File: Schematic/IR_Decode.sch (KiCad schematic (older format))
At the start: 5 parts, among them IC12 74LS574, IC13 74LS161-wkt, IC14 AT27C1024-70PU, IC15 74LS139, IC16 74LS138

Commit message: Fixed up some schematic DCN mistakes and also a few minor typos and diagram issues.
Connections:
- net GND: now also IC12.1 (OE), IC12.10 (Gnd), IC13.8 (Gnd), IC14.11 (GND), IC14.2 (~CE), IC14.20 (~OE), IC14.30 (GND_1), IC14.34 (A12), IC14.35 (A13), IC14.36 (A14), IC14.37 (A15), IC16.4 (E1), IC16.5 (E2)
- removed net GNDREF: IC12.1 (OE), IC12.10 (Gnd), IC13.8 (Gnd), IC14.11 (GND), IC14.2 (~CE), IC14.20 (~OE), IC14.30 (GND_1), IC14.34 (A12), IC14.35 (A13), IC14.36 (A14), IC14.37 (A15), IC15.1 (E), IC16.4 (E1), IC16.5 (E2)
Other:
- note added: "ALUop"
- note added: "DataBus"
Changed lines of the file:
@@
 Entry Wire Line
 	6400 3600 6500 3700
-Text GLabel 6700 4300 2    60   Input ~ 0
-ALUop
+Text GLabel 6600 4300 2    60   Input ~ 0
+Op[0..4]
 Text Label 6000 4000 0    60   ~ 0
 Op0
@@
 	6500 3700 6500 4300
 Wire Bus Line
-	6500 4300 6700 4300
+	6500 4300 6600 4300
 Wire Wire Line
 	5900 3600 6400 3600
@@
 Wire Bus Line
 	1700 2500 1200 2500
-Text GLabel 1200 2500 0    60   Input ~ 0
-DataBus
 Text Label 1850 3600 0    60   ~ 0
 d0
@@
 uSequence\n  Counter
 $Comp
-L GNDREF #PWR043
+L GNDREF #PWR033
 U 1 1 5C99C89C
 P 7250 2250
-F 0 "#PWR043" H 7250 2000 50  0001 C CNN
+F 0 "#PWR033" H 7250 2000 50  0001 C CNN
 F 1 "GNDREF" H 7250 2100 50  0000 C CNN
 F 2 "" H 7250 2250 50  0001 C CNN
@@
 $EndComp
 $Comp
-L GNDREF #PWR044
+L GNDREF #PWR034
 U 1 1 5C99C8B7
 P 3750 3900
-F 0 "#PWR044" H 3750 3650 50  0001 C CNN
+F 0 "#PWR034" H 3750 3650 50  0001 C CNN
 F 1 "GNDREF" H 3750 3750 50  0000 C CNN
 F 2 "" H 3750 3900 50  0001 C CNN
@@
 $EndComp
 $Comp
-L GNDREF #PWR045
+L GNDREF #PWR035
 U 1 1 5C99C8CB
 P 3750 5700
-F 0 "#PWR045" H 3750 5450 50  0001 C CNN
+F 0 "#PWR035" H 3750 5450 50  0001 C CNN
 F 1 "GNDREF" H 3750 5550 50  0000 C CNN
 F 2 "" H 3750 5700 50  0001 C CNN
@@
 $EndComp
 $Comp
-L VCC #PWR046
+L VCC #PWR036
 U 1 1 5C99C8DE
 P 3750 3800
-F 0 "#PWR046" H 3750 3650 50  0001 C CNN
+F 0 "#PWR036" H 3750 3650 50  0001 C CNN
 F 1 "VCC" H 3750 3950 50  0000 C CNN
 F 2 "" H 3750 3800 50  0001 C CNN
@@
 $EndComp
 $Comp
-L VCC #PWR047
+L VCC #PWR037
 U 1 1 5C99C8F9
 P 3750 5600
-F 0 "#PWR047" H 3750 5450 50  0001 C CNN
+F 0 "#PWR037" H 3750 5450 50  0001 C CNN
 F 1 "VCC" H 3750 5750 50  0000 C CNN
 F 2 "" H 3750 5600 50  0001 C CNN
@@
 $EndComp
 $Comp
-L VCC #PWR048
+L VCC #PWR038
 U 1 1 5C99C910
 P 6150 1950
-F 0 "#PWR048" H 6150 1800 50  0001 C CNN
+F 0 "#PWR038" H 6150 1800 50  0001 C CNN
 F 1 "VCC" H 6150 2100 50  0000 C CNN
 F 2 "" H 6150 1950 50  0001 C CNN
@@
 NoConn ~ 2200 5150
 $Comp
-L VCC #PWR049
+L VCC #PWR039
 U 1 1 5C99CB09
 P 1850 5150
-F 0 "#PWR049" H 1850 5000 50  0001 C CNN
+F 0 "#PWR039" H 1850 5000 50  0001 C CNN
 F 1 "VCC" H 1850 5300 50  0000 C CNN
 F 2 "" H 1850 5150 50  0001 C CNN
@@
 JumpZ
 $Comp
-L GNDREF #PWR050
+L GNDREF #PWR040
 U 1 1 5C99F486
 P 4150 2700
-F 0 "#PWR050" H 4150 2450 50  0001 C CNN
+F 0 "#PWR040" H 4150 2450 50  0001 C CNN
 F 1 "GNDREF" H 4150 2550 50  0000 C CNN
 F 2 "" H 4150 2700 50  0001 C CNN
@@
 NoConn ~ 4800 2250
 $Comp
-L VCC #PWR051
+L VCC #PWR041
 U 1 1 5C99F6F5
 P 4400 1900
-F 0 "#PWR051" H 4400 1750 50  0001 C CNN
+F 0 "#PWR041" H 4400 1750 50  0001 C CNN
 F 1 "VCC" H 4400 2050 50  0000 C CNN
 F 2 "" H 4400 1900 50  0001 C CNN
@@
 $EndComp
 Wire Wire Line
-	4800 2150 4400 2150
-Wire Wire Line
-	4400 2150 4400 1900
+	4400 2150 4800 2150
+Wire Wire Line
+	4400 1900 4400 2150
 $Comp
 L 74LS139 IC15
@@
 Text Notes 8750 3400 0    60   ~ 0
 Databus\nWriter\ndemux
-Text Notes 8550 5650 0    60   ~ 0
+Text Notes 8600 5750 0    60   ~ 0
 Databus\nReader\ndemux
 $Comp
-L GNDREF #PWR052
+L GNDREF #PWR042
 U 1 1 5C99920E
-P 7850 3550
-F 0 "#PWR052" H 7850 3300 50  0001 C CNN
-F 1 "GNDREF" H 7850 3400 50  0000 C CNN
-F 2 "" H 7850 3550 50  0001 C CNN
-F 3 "" H 7850 3550 50  0001 C CNN
-	1    7850 3550
-	1    0    0    -1
-$EndComp
-Wire Wire Line
-	8050 3550 7850 3550
+P 8000 3900
+F 0 "#PWR042" H 8000 3650 50  0001 C CNN
+F 1 "GNDREF" H 8000 3750 50  0000 C CNN
+F 2 "" H 8000 3900 50  0001 C CNN
+F 3 "" H 8000 3900 50  0001 C CNN
+	1    8000 3900
+	1    0    0    -1
+$EndComp
 $Comp
 L 74LS138 IC16
 U 1 1 5C9992C4
 P 8700 4900
-F 0 "IC16" H 8700 5500 50  0000 C CNN
-F 1 "74LS138" H 8700 5400 50  0000 C CNN
+F 0 "IC16" H 8700 5700 50  0000 C CNN
+F 1 "74LS138" H 8700 5600 50  0000 C CNN
 F 2 "" H 8700 4900 50  0001 C CNN
 F 3 "" H 8700 4900 50  0001 C CNN
@@
 	7150 4550 8100 4550
 $Comp
-L GNDREF #PWR053
+L GNDREF #PWR043
 U 1 1 5C99955D
-P 7850 5250
-F 0 "#PWR053" H 7850 5000 50  0001 C CNN
-F 1 "GNDREF" H 7850 5100 50  0000 C CNN
-F 2 "" H 7850 5250 50  0001 C CNN
-F 3 "" H 7850 5250 50  0001 C CNN
-	1    7850 5250
+P 7850 5550
+F 0 "#PWR043" H 7850 5300 50  0001 C CNN
+F 1 "GNDREF" H 7850 5400 50  0000 C CNN
+F 2 "" H 7850 5550 50  0001 C CNN
+F 3 "" H 7850 5550 50  0001 C CNN
+	1    7850 5550
 	1    0    0    -1
 $EndComp
@@
 Connection ~ 8000 5250
 $Comp
-L VCC #PWR054
+L VCC #PWR044
 U 1 1 5C999650
 P 7850 5050
-F 0 "#PWR054" H 7850 4900 50  0001 C CNN
+F 0 "#PWR044" H 7850 4900 50  0001 C CNN
 F 1 "VCC" H 7850 5200 50  0000 C CNN
 F 2 "" H 7850 5050 50  0001 C CNN
@@
 	8100 5050 7850 5050
 $Comp
-L GNDREF #PWR055
+L GNDREF #PWR045
 U 1 1 5C9996EE
 P 2000 3900
-F 0 "#PWR055" H 2000 3650 50  0001 C CNN
+F 0 "#PWR045" H 2000 3650 50  0001 C CNN
 F 1 "GNDREF" H 2000 3750 50  0000 C CNN
 F 2 "" H 2000 3900 50  0001 C CNN
@@
 Wire Wire Line
 	4800 2700 4650 2700
+Text GLabel 1200 2500 0    60   Input ~ 0
+d[0..7]
+Text Notes 1300 2450 0    60   ~ 0
+DataBus
+Text Notes 6200 4200 0    60   ~ 0
+ALUop
+$Comp
+L VCC #PWR046
+U 1 1 5C9AFDC5
+P 9100 4300
+F 0 "#PWR046" H 9100 4150 50  0001 C CNN
+F 1 "VCC" H 9100 4450 50  0000 C CNN
+F 2 "" H 9100 4300 50  0001 C CNN
+F 3 "" H 9100 4300 50  0001 C CNN
+	1    9100 4300
+	1    0    0    -1
+$EndComp
+Wire Wire Line
+	8700 4450 8700 4300
+Wire Wire Line
+	8700 4300 9100 4300
+Wire Wire Line
+	7850 5550 7850 5250
+Wire Wire Line
+	8700 5350 8700 5450
+Wire Wire Line
+	8700 5450 7850 5450
+Connection ~ 7850 5450
+$Comp
+L VCC #PWR047
+U 1 1 5C9B044B
+P 7700 3500
+F 0 "#PWR047" H 7700 3350 50  0001 C CNN
+F 1 "VCC" H 7700 3650 50  0000 C CNN
+F 2 "" H 7700 3500 50  0001 C CNN
+F 3 "" H 7700 3500 50  0001 C CNN
+	1    7700 3500
+	1    0    0    -1
+$EndComp
+Wire Wire Line
+	8000 3900 8000 3350
+Wire Wire Line
+	8000 3350 8050 3350
+Wire Wire Line
+	8150 3650 8000 3650
+Connection ~ 8000 3650
+Wire Wire Line
+	8150 3550 7700 3550
+Wire Wire Line
+	7700 3550 7700 3500
 $EndSCHEMATC

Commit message: Generated a new schematic of the circuit
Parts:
- IC15: symbol 74LS139 -> 74LS139-RESCUE-Schematic
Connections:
- net GND: now also IC15.1 (E)
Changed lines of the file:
@@
 EESchema Schematic File Version 2
+LIBS:Schematic-rescue
 LIBS:power
 LIBS:device
@@
 LIBS:7400-ic
 LIBS:74LS593
+LIBS:74LS139
 LIBS:Schematic-cache
 EELAYER 25 0
@@
 	4400 1900 4400 2150
 $Comp
-L 74LS139 IC15
+L 74LS139-RESCUE-Schematic IC15
 U 1 1 5C990E8F
 P 8900 3300
+AR Path="/5C990E8F" Ref="IC15"  Part="1"
+AR Path="/5C9850E7/5C990E8F" Ref="IC15"  Part="1"
 F 0 "IC15" H 8900 3850 50  0000 C CNN
 F 1 "74LS139" H 8900 3750 50  0000 C CNN

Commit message: Working on the PCB
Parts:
- IC12: footprint (none) -> Housings_DIP:DIP-20_W7.62mm_Socket
- IC13, IC15, IC16: footprint (none) -> Housings_DIP:DIP-16_W7.62mm_Socket
- IC14: footprint DIP1556W56P254L5232H483Q40N -> Housings_DIP:DIP-40_W25.4mm_Socket
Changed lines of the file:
@@
 F 0 "IC12" H 2900 4100 50  0000 C CNN
 F 1 "74LS574" H 2900 4000 50  0000 C CNN
-F 2 "" H 2900 3400 50  0001 C CNN
+F 2 "Housings_DIP:DIP-20_W7.62mm_Socket" H 2900 3400 50  0001 C CNN
 F 3 "" H 2900 3400 50  0001 C CNN
 	1    2900 3400
@@
 F 0 "IC15" H 8900 3850 50  0000 C CNN
 F 1 "74LS139" H 8900 3750 50  0000 C CNN
-F 2 "" H 8900 3300 50  0001 C CNN
+F 2 "Housings_DIP:DIP-16_W7.62mm_Socket" H 8900 3300 50  0001 C CNN
 F 3 "" H 8900 3300 50  0001 C CNN
 	1    8900 3300
@@
 F 0 "IC13" H 2900 5900 50  0000 C CNN
 F 1 "74LS161-wkt" H 2900 5800 50  0000 C CNN
-F 2 "" H 2900 5200 50  0001 C CNN
+F 2 "Housings_DIP:DIP-16_W7.62mm_Socket" H 2900 5200 50  0001 C CNN
 F 3 "" H 2900 5200 50  0001 C CNN
 	1    2900 5200
@@
 F 0 "IC16" H 8700 5700 50  0000 C CNN
 F 1 "74LS138" H 8700 5600 50  0000 C CNN
-F 2 "" H 8700 4900 50  0001 C CNN
+F 2 "Housings_DIP:DIP-16_W7.62mm_Socket" H 8700 4900 50  0001 C CNN
 F 3 "" H 8700 4900 50  0001 C CNN
 	1    8700 4900
@@
 F 0 "IC14" H 5350 2300 50  0000 L CNN
 F 1 "AT27C1024-70PU" H 5050 2200 50  0000 L CNN
-F 2 "DIP1556W56P254L5232H483Q40N" H 5750 2150 50  0001 L CNN
+F 2 "Housings_DIP:DIP-40_W25.4mm_Socket" H 5750 2150 50  0001 L CNN
 F 3 "http://www.atmel.com/images/doc0019.pdf" H 5750 2050 50  0001 L CNN
 F 4 "AT27C1024-70PU,  OTP EPROM Memory 1Mbit 64K x 16 bit 70ns 4.5  5.5 V 40-Pin PDIP" H 5750 1950 50  0001 L CNN "Description"

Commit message: Brought the schematic and PCB board design up to date.
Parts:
- added IC17: 74LS04, Housings_DIP:DIP-14_W7.62mm_Socket, symbol 74LS04
- added J4: uSeq Pin Header, Socket_Strips:Socket_Strip_Straight_1x06_Pitch2.54mm, symbol Conn_01x06_Male
- added J5: IR Pin Header, Socket_Strips:Socket_Strip_Straight_1x10_Pitch2.54mm, symbol Conn_01x10_Male
- IC12: value 74LS574 -> 74HCT574
- IC13: value 74LS161-wkt -> 74HCT161
- IC14: footprint Housings_DIP:DIP-40_W25.4mm_Socket -> Housings_DIP:DIP-40_W15.24mm_Socket
- IC15: value 74LS139 -> 74HCT139
- IC16: value 74LS138 -> 74HCT138
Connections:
- net AHload: now also IC17.8; no longer IC16.10 (O5)
- net ALload: now also IC17.10; no longer IC16.9 (O6)
- net Aload: now also IC17.4; no longer IC16.13 (O2)
- net Bload: now also IC17.6; no longer IC16.12 (O3)
- net GND: now also IC17.7 (GND), IC17.7 (GND), IC17.7 (GND), IC17.7 (GND), IC17.7 (GND); no longer IC12.1 (OE), IC14.2 (~CE), IC14.20 (~OE), IC14.34 (A12), IC14.35 (A13), IC14.36 (A14), IC14.37 (A15), IC15.1 (E), IC16.4 (E1), IC16.5 (E2)
- net IRload: now also IC17.2; no longer IC16.14 (O1)
- net PCincr: now also IC14.4 (O14); no longer IC14.5 (O13)
- net VCC: now also IC17.14 (VCC), IC17.14 (VCC), IC17.14 (VCC), IC17.14 (VCC), IC17.14 (VCC); no longer IC13.10 (Cet), IC13.7 (Cep), IC13.9 (~Pe), IC14.1 (VPP), IC14.39 (~PGM), IC16.6 (E3)
- net at IC12.12 (Q7), IC14.33 (A11): now also J5.10 (Pin_10)
- net at IC12.13 (Q6), IC14.32 (A10): now also J5.9 (Pin_9)
- net at IC12.14 (Q5), IC14.31 (A9): now also J5.8 (Pin_8)
- net at IC12.15 (Q4), IC14.29 (A8): now also J5.7 (Pin_7)
- net at IC12.16 (Q3), IC14.28 (A7): now also J5.6 (Pin_6)
- net at IC12.17 (Q2), IC14.27 (A6): now also J5.5 (Pin_5)
- net at IC12.18 (Q1), IC14.26 (A5): now also J5.4 (Pin_4)
- net at IC12.19 (Q0), IC14.25 (A4): now also J5.3 (Pin_3)
- net at IC13.14 (Q0), IC14.21 (A0): now also J4.3 (Pin_3)
- net at IC13.13 (Q1), IC14.22 (A1): now also J4.4 (Pin_4)
- net at IC13.12 (Q2), IC14.23 (A2): now also J4.5 (Pin_5)
- net at IC13.11 (Q3), IC14.24 (A3): now also J4.6 (Pin_6)
- net ~uSreset: now reaches IC14.3 (O15)
- net ~uSreset: now also IC13.1 (~MR)
- net ALUresult renamed ~ALUresult
- net ARena renamed JumpOp2
- net IOload renamed ~IOload
- net JumpC renamed JumpOp0
- net JumpZ renamed JumpOp1
- net MEMload: no longer names the net of IC16.11 (O4)
- net MEMload: now also IC17.9
- net MEMresult renamed ~MEMresult
- net UARTresult renamed ~UARTresult
- removed net uSreset: IC13.1 (~MR), IC14.4 (O14)
- new net: IC16.10 (O5), IC17.11
- new net: IC16.12 (O3), IC17.5
- new net: IC16.13 (O2), IC17.3
- new net: IC16.14 (O1), IC17.1
- new net Hi: IC13.10 (Cet), IC13.7 (Cep), IC13.9 (~Pe), IC14.1 (VPP), IC14.39 (~PGM), IC16.6 (E3)
- new net Lo: IC12.1 (OE), IC14.2 (~CE), IC14.20 (~OE), IC14.34 (A12), IC14.35 (A13), IC14.36 (A14), IC14.37 (A15), IC15.1 (E), IC16.4 (E1), IC16.5 (E2), J4.1 (Pin_1), J5.1 (Pin_1)
- new net ~ARena: IC14.5 (O13)
- new net ~MEMload: IC16.9 (O6)
- no-connect marks 9 -> 10
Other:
- note added: "CSCvon8 is a microsequenced CPU. The Instruction register, combined with the microsequence counter, selects the next microinstruction to perform.\nThis is "looked up" in the Decode ROM, which produces the sixteen control lines for the specific microinstruction. The ALUop goes to the ALU. The\nJumpOp goes to the Jump logic. The three LoadOp lines are demultiplexed to choose one device to load from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"
- note added: "It's so annoying that the 74HCT574 has an active high load line,\nand the RAM and UART have active low load lines. One extra\nchip just to deal with that, sigh."
- moved on the sheet: IC12, IC16

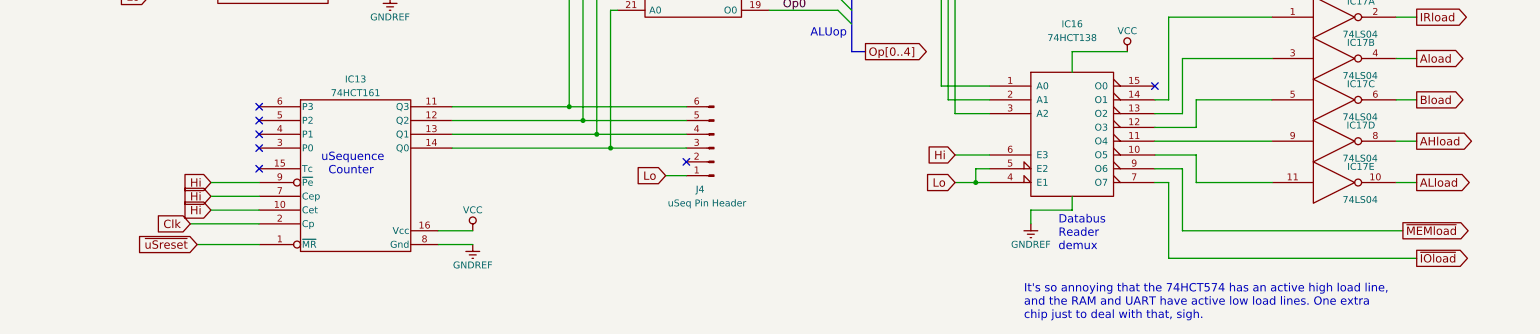
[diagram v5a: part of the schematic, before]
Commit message: Brought the schematic up to date with the wiring from the TTL verilog version.
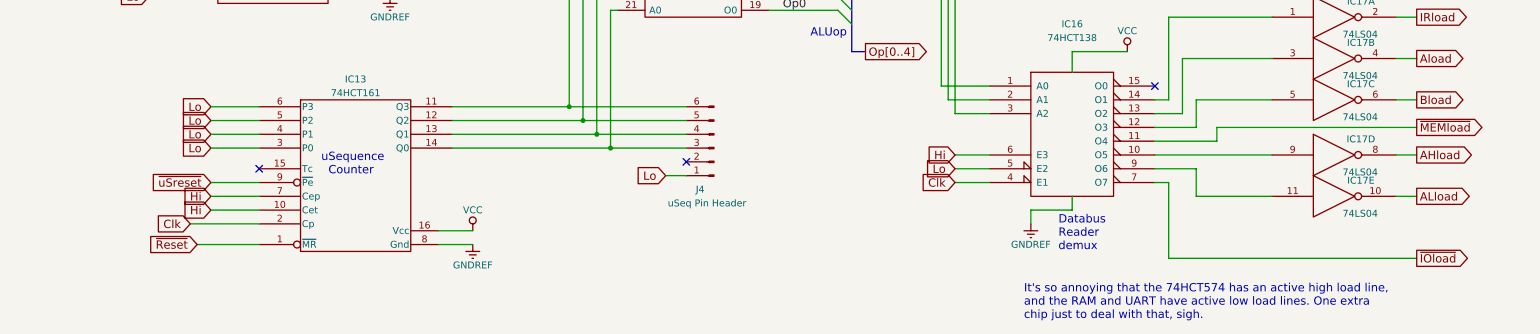
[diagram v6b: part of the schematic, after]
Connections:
- net Clk: now also IC16.4 (E1)
- net Hi: no longer IC13.9 (~Pe)
- net Lo: now also IC13.3 (P0), IC13.4 (P1), IC13.5 (P2), IC13.6 (P3); no longer IC16.4 (E1)
- net ~MEMload: now also IC16.11 (O4); no longer IC16.9 (O6)
- net ~uSreset: now also IC13.9 (~Pe); no longer IC13.1 (~MR)
- net at IC16.10 (O5): now also IC17.9; no longer IC17.11
- new net: IC16.9 (O6), IC17.11
- new net ~Reset: IC13.1 (~MR)
- no-connect marks 10 -> 6
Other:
- moved on the sheet: IC17D, IC17E
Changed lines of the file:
@@
 Text Label 1250 2900 0    60   ~ 0
 d7
-Text GLabel 1750 5700 0    60   Input ~ 0
+Text GLabel 1850 5250 0    60   Input ~ 0
 ~uSreset
-NoConn ~ 2200 4700
-NoConn ~ 2200 4800
-NoConn ~ 2200 4900
-NoConn ~ 2200 5000
 Text Notes 5200 3550 0    60   ~ 0
 Decode\n ROM
@@
 	1    0    0    -1
 $EndComp
-NoConn ~ 2200 5150
 Text GLabel 1700 5550 0    60   Input ~ 0
 Clk
@@
 Text GLabel 10600 4650 2    60   Output ~ 0
 Bload
-Text GLabel 10500 5600 2    60   Output ~ 0
+Text GLabel 10600 4850 2    60   Output ~ 0
 ~MEMload
-Text GLabel 10600 4950 2    60   Output ~ 0
+Text GLabel 10600 5050 2    60   Output ~ 0
 AHload
-Text GLabel 10600 5250 2    60   Output ~ 0
+Text GLabel 10600 5350 2    60   Output ~ 0
 ALload
 Text GLabel 10600 5800 2    60   Output ~ 0
@@
 Text GLabel 7900 3350 0    60   Input ~ 0
 Lo
-Text GLabel 7250 5250 0    60   Input ~ 0
+Text GLabel 7250 5150 0    60   Input ~ 0
 Lo
 Text GLabel 7250 5050 0    60   Input ~ 0
@@
 Text Notes 1000 1350 0    60   ~ 0
 CSCvon8 is a microsequenced CPU. The Instruction register, combined with the microsequence counter, selects the next microinstruction to perform.\nThis is "looked up" in the Decode ROM, which produces the sixteen control lines for the specific microinstruction. The ALUop goes to the ALU. The\nJumpOp goes to the Jump logic. The three LoadOp lines are demultiplexed to choose one device to load from the databus. The two DbusOp lines are\ndemultiplexed to choose one device to write onto the databus.\n\nNormally, the microsequence counter increments, but if uSreset goes low it will reset back to value zero. All microsequences have their "zero"\nmicroinstruction to load the Instruction register from the data bus (ROM or RAM) and to increment the Instruction register.
-Text GLabel 1850 5250 0    60   Input ~ 0
-Hi
 Text GLabel 1850 5350 0    60   Input ~ 0
 Hi
@@
 L 74LS04 IC17
 U 4 1 5CA2E1D7
-P 10000 4950
-F 0 "IC17" H 10195 5065 50  0000 C CNN
-F 1 "74LS04" H 10190 4825 50  0000 C CNN
-F 2 "Housings_DIP:DIP-14_W7.62mm_Socket" H 10000 4950 50  0001 C CNN
-F 3 "" H 10000 4950 50  0001 C CNN
-	4    10000 4950
+P 10000 5050
+F 0 "IC17" H 10195 5165 50  0000 C CNN
+F 1 "74LS04" H 10190 4925 50  0000 C CNN
+F 2 "Housings_DIP:DIP-14_W7.62mm_Socket" H 10000 5050 50  0001 C CNN
+F 3 "" H 10000 5050 50  0001 C CNN
+	4    10000 5050
 	1    0    0    -1
 $EndComp
@@
 L 74LS04 IC17
 U 5 1 5CA2E289
-P 10000 5250
-F 0 "IC17" H 10195 5365 50  0000 C CNN
-F 1 "74LS04" H 10190 5125 50  0000 C CNN
-F 2 "Housings_DIP:DIP-14_W7.62mm_Socket" H 10000 5250 50  0001 C CNN
-F 3 "" H 10000 5250 50  0001 C CNN
-	5    10000 5250
+P 10000 5350
+F 0 "IC17" H 10195 5465 50  0000 C CNN
+F 1 "74LS04" H 10190 5225 50  0000 C CNN
+F 2 "Housings_DIP:DIP-14_W7.62mm_Socket" H 10000 5350 50  0001 C CNN
+F 3 "" H 10000 5350 50  0001 C CNN
+	5    10000 5350
 	1    0    0    -1
 $EndComp
@@
 	7250 5250 7500 5250
 Wire Wire Line
-	7500 5150 7400 5150
-Wire Wire Line
-	7400 5150 7400 5250
-Connection ~ 7400 5250
+	7250 5150 7500 5150
 Wire Wire Line
 	7500 5050 7250 5050
@@
 	8800 5250 8700 5250
 Wire Wire Line
-	10500 5600 8900 5600
-Wire Wire Line
-	8900 5600 8900 5150
-Wire Wire Line
-	8900 5150 8700 5150
-Wire Wire Line
-	9000 5050 8700 5050
-Wire Wire Line
-	9550 5250 9000 5250
-Wire Wire Line
-	9000 5250 9000 5050
-Wire Wire Line
-	9550 4950 8700 4950
+	8700 5150 9000 5150
+Wire Wire Line
+	8700 5050 9550 5050
 Wire Wire Line
 	9550 4050 8800 4050
@@
 	9000 4850 8700 4850
 Wire Wire Line
-	10600 5250 10450 5250
-Wire Wire Line
-	10600 4950 10450 4950
+	10600 5350 10450 5350
+Wire Wire Line
+	10600 5050 10450 5050
 Wire Wire Line
 	10600 4650 10450 4650
@@
 	4100 1950 4100 1900
 NoConn ~ 4000 1900
+Text GLabel 1850 4700 0    60   Input ~ 0
+Lo
+Text GLabel 1850 4800 0    60   Input ~ 0
+Lo
+Text GLabel 1850 4900 0    60   Input ~ 0
+Lo
+Text GLabel 1850 5000 0    60   Input ~ 0
+Lo
+Wire Wire Line
+	1850 4700 2200 4700
+Wire Wire Line
+	1850 4800 2200 4800
+Wire Wire Line
+	1850 4900 2200 4900
+Wire Wire Line
+	1850 5000 2200 5000
+Text GLabel 1750 5700 0    60   Input ~ 0
+~Reset
+NoConn ~ 2200 5150
+Text GLabel 7250 5250 0    60   Input ~ 0
+Clk
+Wire Wire Line
+	9000 5150 9000 5350
+Wire Wire Line
+	9000 5350 9550 5350
+Wire Wire Line
+	8700 4950 9150 4950
+Wire Wire Line
+	9150 4950 9150 4850
+Wire Wire Line
+	9150 4850 10600 4850
 $EndSCHEMATC

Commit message: Updated the schematic and also moved to KiCad 5.
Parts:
- removed IC15: 74HCT139, Housings_DIP:DIP-16_W7.62mm_Socket, symbol 74LS139-RESCUE-Schematic
- removed J4: uSeq Pin Header, Socket_Strips:Socket_Strip_Straight_1x06_Pitch2.54mm, symbol Conn_01x06_Male
- removed J5: IR Pin Header, Socket_Strips:Socket_Strip_Straight_1x10_Pitch2.54mm, symbol Conn_01x10_Male
- added IC15: 74HCT139, Package_DIP:DIP-16_W7.62mm_Socket, symbol 74xx:74LS139
- added unit 7 of IC17
- added J4: uSeq Pin Header, Connector_PinSocket_2.54mm:PinSocket_1x06_P2.54mm_Vertical, symbol Connector:Conn_01x06_Female
- added J5: IR Pin Header, Connector_PinSocket_2.54mm:PinSocket_1x10_P2.54mm_Vertical, symbol Connector:Conn_01x10_Female
- IC12: symbol 74LS574-RESCUE-Schematic -> 74LS593:74LS574-RESCUE-Schematic
- IC13: symbol 74LS161-wkt -> 74LS593:74LS161-wkt
- IC14: symbol AT27C1024-70PU -> AT27C1024-70PU:AT27C1024-70PU
- IC16: symbol 74LS138 -> 74xx:74LS138
- IC17: value 74LS04 -> 74HCT04; symbol 74LS04 -> 74xx:74LS04
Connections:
- net DbusOp0: now also IC15.2 (A0)
- net DbusOp1: now also IC15.3 (A1)
- net Lo: now also IC15.1 (E), J4.6 (Pin_6), J5.10 (Pin_10)
- net VCC: now also IC15.16 (VCC), IC17.14 (VCC); no longer IC17.14 (VCC), IC17.14 (VCC), IC17.14 (VCC), IC17.14 (VCC), IC17.14 (VCC)
- net ~ALUresult: now also IC15.5 (O1)
- net ~MEMresult: now also IC15.4 (O0)
- net ~UARTresult: now also IC15.6 (O2)
- net at IC12.12 (Q7), IC14.33 (A11): now also J5.1 (Pin_1)
- net at IC12.13 (Q6), IC14.32 (A10): now also J5.2 (Pin_2)
- net at IC12.14 (Q5), IC14.31 (A9): now also J5.3 (Pin_3)
- net at IC12.15 (Q4), IC14.29 (A8): now also J5.4 (Pin_4)
- net at IC12.16 (Q3), IC14.28 (A7): now also J5.5 (Pin_5)
- net at IC12.17 (Q2), IC14.27 (A6): now also J5.6 (Pin_6)
- net at IC12.18 (Q1), IC14.26 (A5): now also J5.7 (Pin_7)
- net at IC12.19 (Q0), IC14.25 (A4): now also J5.8 (Pin_8)
- net at IC13.14 (Q0), IC14.21 (A0): now also J4.4 (Pin_4)
- net at IC13.13 (Q1), IC14.22 (A1): now also J4.3 (Pin_3)
- net at IC13.12 (Q2), IC14.23 (A2): now also J4.2 (Pin_2)
- net at IC13.11 (Q3), IC14.24 (A3): now also J4.1 (Pin_1)
- net GND renamed GNDREF
- net GNDREF: now also IC15.8 (GND), IC17.7 (GND); no longer IC17.7 (GND), IC17.7 (GND), IC17.7 (GND), IC17.7 (GND), IC17.7 (GND)
